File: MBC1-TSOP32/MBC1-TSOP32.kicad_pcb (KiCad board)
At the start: 2 copper layers, 13.5 x 21.7 mm, 4 parts

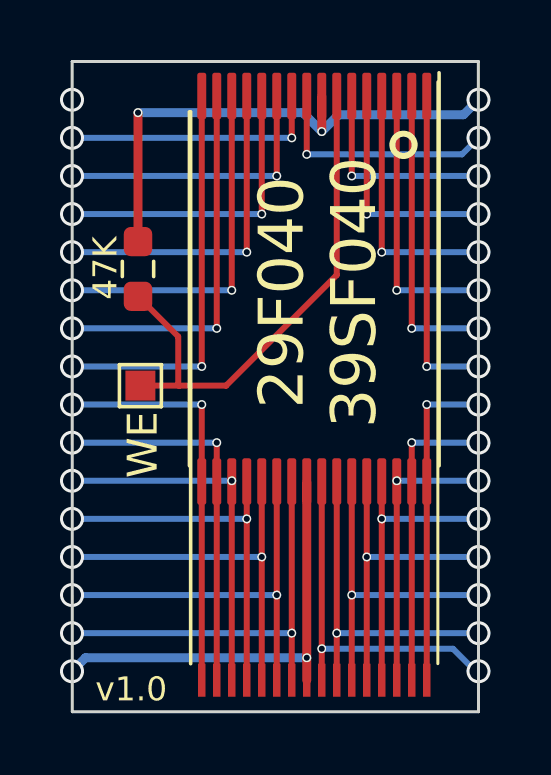
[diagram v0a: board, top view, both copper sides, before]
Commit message: Updated via size to reduce production costs
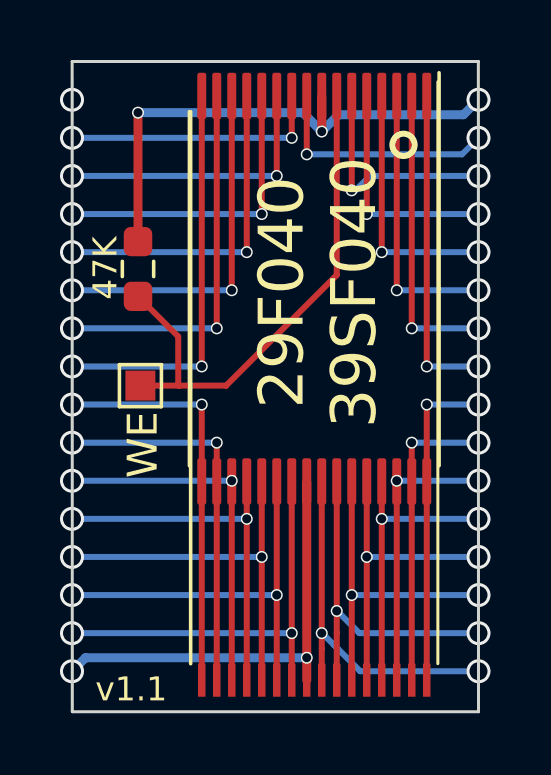
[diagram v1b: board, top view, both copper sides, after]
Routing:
- net A17: track 6.81 -> 7.50 mm
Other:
- board text added: "v1.1"
- board text removed: "v1.0"
